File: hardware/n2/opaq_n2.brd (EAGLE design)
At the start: 30.3 x 50.4 mm, 41 parts, among them IC1 RT9013-XXXB, IC2 TS5A3157, IC3 ATSHA204_SOIC8, IC4 ACS712, IC5 ADS1100, IC6 ATMega-328, IC7 AT25F512BWIDE_5.3MM, IC8 LM2594HV, K1 62101021021, X1 16 MHz

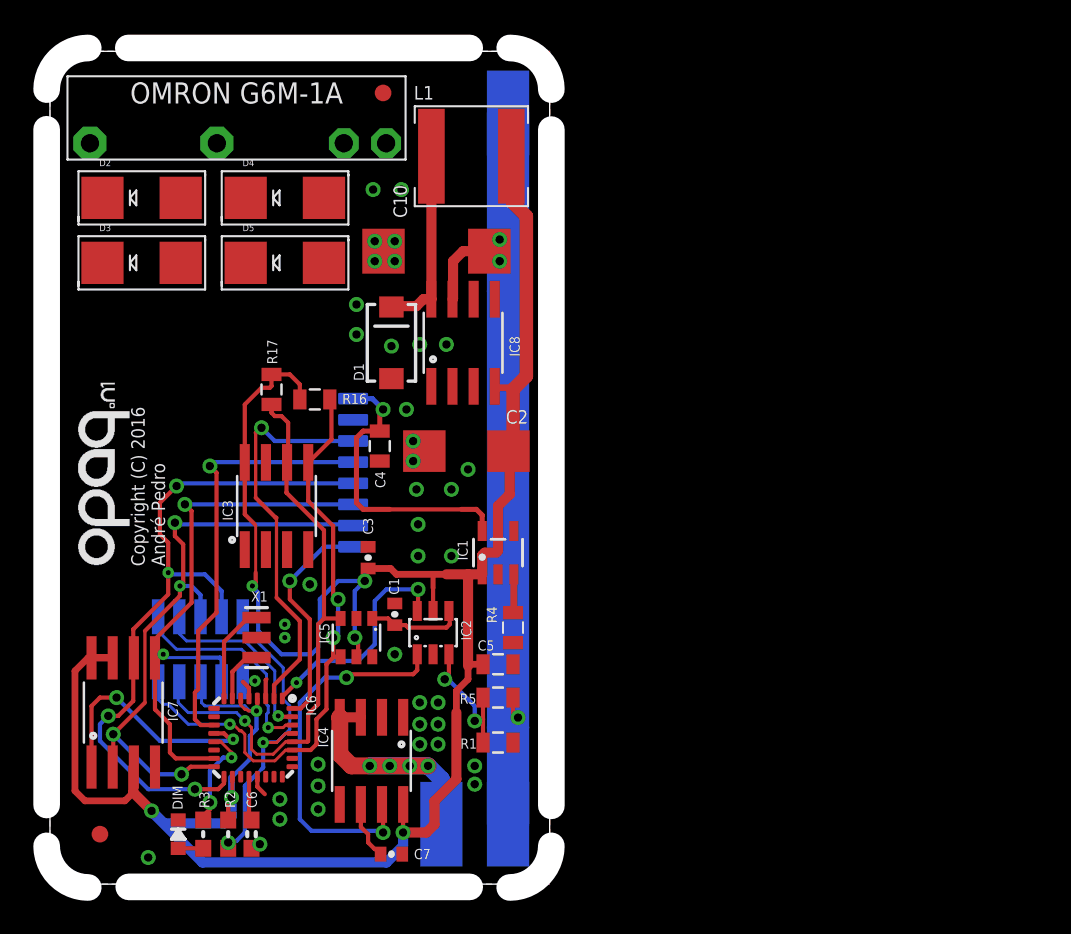
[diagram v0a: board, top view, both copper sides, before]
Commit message: Updated the Opaq n1 firmware to read the external temperature and the input voltage. Added the support for the external flash. Renamed the folder of the Opaq n1 hardware.
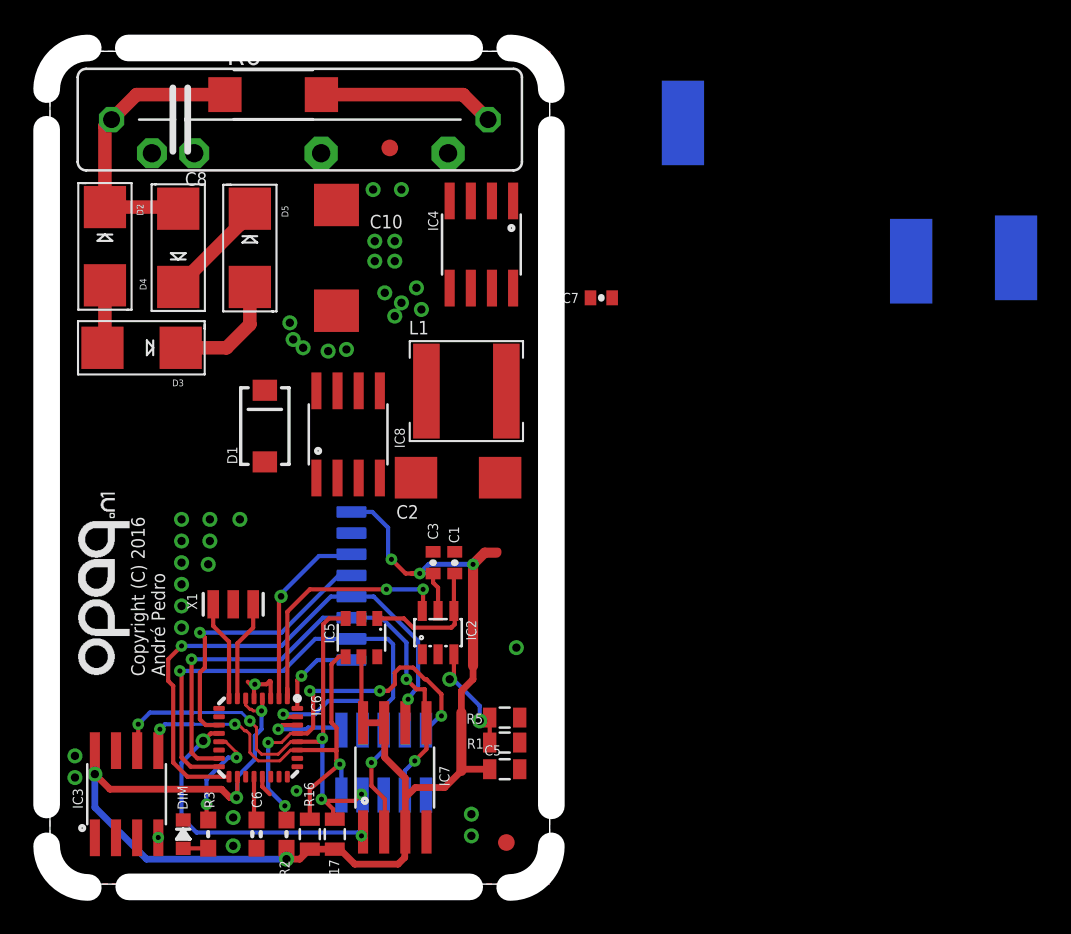
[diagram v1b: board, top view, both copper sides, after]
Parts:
- removed C4: 0.1uF, SparkFun-Passives:0805
- removed IC1: RT9013-XXXB, v-reg_extra:SOT23-5
- removed R4: (no value), resistor:0805
- added C8: (no value), resistor:C225-062X268
- added R6: (no value), resistor:R2512W
- moved VPLUS_IN 45.7 mm to (58.0, 37.6)
- moved GND 44.0 mm to (51.7, 37.4)
- moved C7 35.7 mm to (33.1, 35.2), turned to 180 degrees
- moved IC4 31.7 mm to (25.9, 38.4)
- moved R17 27.0 mm to (17.1, 3.00), turned to 270 degrees
- moved R16 26.1 mm to (15.6, 3.00), turned to 270 degrees
- moved JP1 24.4 mm to (27.4, 2.50)
- moved IC3 19.5 mm to (4.60, 5.40)
- moved IC7 16.8 mm to (20.7, 6.40)
- moved L1 14.1 mm to (25.0, 29.6)
- moved K1 12.9 mm to (19.4, 7.30)
- moved VPLUS_OUT 10.5 mm to (38.0, 45.7)
- moved D1 9.10 mm to (12.9, 27.5)
- moved IC8 8.82 mm to (17.9, 27.0)
- moved D4 7.07 mm to (7.70, 38.2), turned to 90 degrees
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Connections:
- removed net +5V: C2.+, C3.1, C5.1, IC1.1, IC2.5, IC3.8, IC4.8, IC5.5, IC8.4, L1.P$1, R16.2, R17.2
- removed net N$10: IC1.3, R4.2
- new net L: C8.2, R6.2
- new net LC: C8.1, D2.C, D4.A, R6.1
- new net N: D3.C, D5.A
- new net V+: D4.C, D5.C
- new net V-: D2.A, D3.A
- net 3.3V: now also C2.+, C3.1, C5.1, IC2.5, IC3.8, IC4.8, IC5.5, IC6.18, IC6.4, IC6.6, IC7.3, IC7.7, IC7.8, IC8.4, L1.P$1, R16.2, R17.2, R2.1; no longer C4.1, IC1.5
- net GND: no longer C4.2, IC1.2, R4.1
- net VCC: no longer IC6.18, IC6.4, IC6.6, IC7.3, IC7.7, IC7.8, R2.1
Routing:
- net +5V: track 111.9 -> 0.00 mm, vias 4 -> 0
- net 3.3V: track 17.7 -> 91.1 mm, vias 1 -> 7
- net VPLUS_IN: track 56.4 -> 0.00 mm, vias 3 -> 0
- net VCC: track 40.2 -> 0.00 mm, vias 3 -> 0
- net CURRENT_VOUT: track 22.9 -> 0.00 mm, vias 2 -> 0
- net LC: track 0.00 -> 17.3 mm
- net GND_IN: track 16.5 -> 0.00 mm, vias 4 -> 0
- net NRF24_CE: track 24.0 -> 12.2 mm
- net N$17: track 11.2 -> 0.00 mm
- net L: track 0.00 -> 10.6 mm
- net A4_SDA: track 36.4 -> 27.2 mm
- net NRF24_CSN: track 26.1 -> 17.3 mm
- net D13_SCK: track 43.1 -> 34.9 mm, vias 4 -> 2
- net D0_RX: track 13.3 -> 5.15 mm
- net NRF24_IRQ: track 13.5 -> 5.45 mm
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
